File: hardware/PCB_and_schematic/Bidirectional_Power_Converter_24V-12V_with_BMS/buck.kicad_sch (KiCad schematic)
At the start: 0 parts

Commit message: Drawning schematic for buck/boost converter
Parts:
- added U2: LM358, symbol Amplifier_Operational:LM358
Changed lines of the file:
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@@
 	(generator_version "8.0")
 	(paper "A4")
+	(symbol
+		(lib_id "Amplifier_Operational:LM358")
+		(at 219.71 140.97 180)
+		(unit 2)
+		(exclude_from_sim no)
+		(in_bom yes)
+		(on_board yes)
+		(dnp no)
+		(fields_autoplaced yes)
+		(property "Reference" "U2"
+			(at 219.71 130.81 0)
+			(effects
+				(font
+					(size 1.27 1.27)
+				)
+			)
+		)
+		(property "Value" "LM358"
+			(at 219.71 133.35 0)
+			(effects
+				(font
+					(size 1.27 1.27)
+				)
+			)
+		)
+		(property "Footprint" ""
+			(at 219.71 140.97 0)
+			(effects
+				(font
+					(size 1.27 1.27)
+				)
+				(hide yes)
+			)
+		)
+		(property "Datasheet" "http://www.ti.com/lit/ds/symlink/lm2904-n.pdf"
+			(at 219.71 140.97 0)
+			(effects
+				(font
+					(size 1.27 1.27)
+				)
+				(hide yes)
+			)
+		)
+		(property "Description" "Low-Power, Dual Operational Amplifiers, DIP-8/SOIC-8/TO-99-8"
+			(at 219.71 140.97 0)
+			(effects
+				(font
+					(size 1.27 1.27)
+				)
+				(hide yes)
+			)
+		)
+		(pin "1"
+		)
+		(pin "6"
+		)
+		(pin "5"
+		)
+		(pin "8"
+		)
+		(pin "3"
+		)
+		(pin "2"
+		)
+		(pin "7"
+		)
+		(pin "4"
+		)
+		(instances
+			(project "Bidirectional_Power_Converter_24V-12V_with_BMS"
+				(path "/57ff2453-26d1-489b-aa83-9af273df178f/81802b0c-d137-483c-9072-3d8784bb4773/ebfaa78a-1358-458a-b207-86dd3b22cb8b"
+					(reference "U2")
+					(unit 2)
+				)
+			)
+		)
+	)
 )

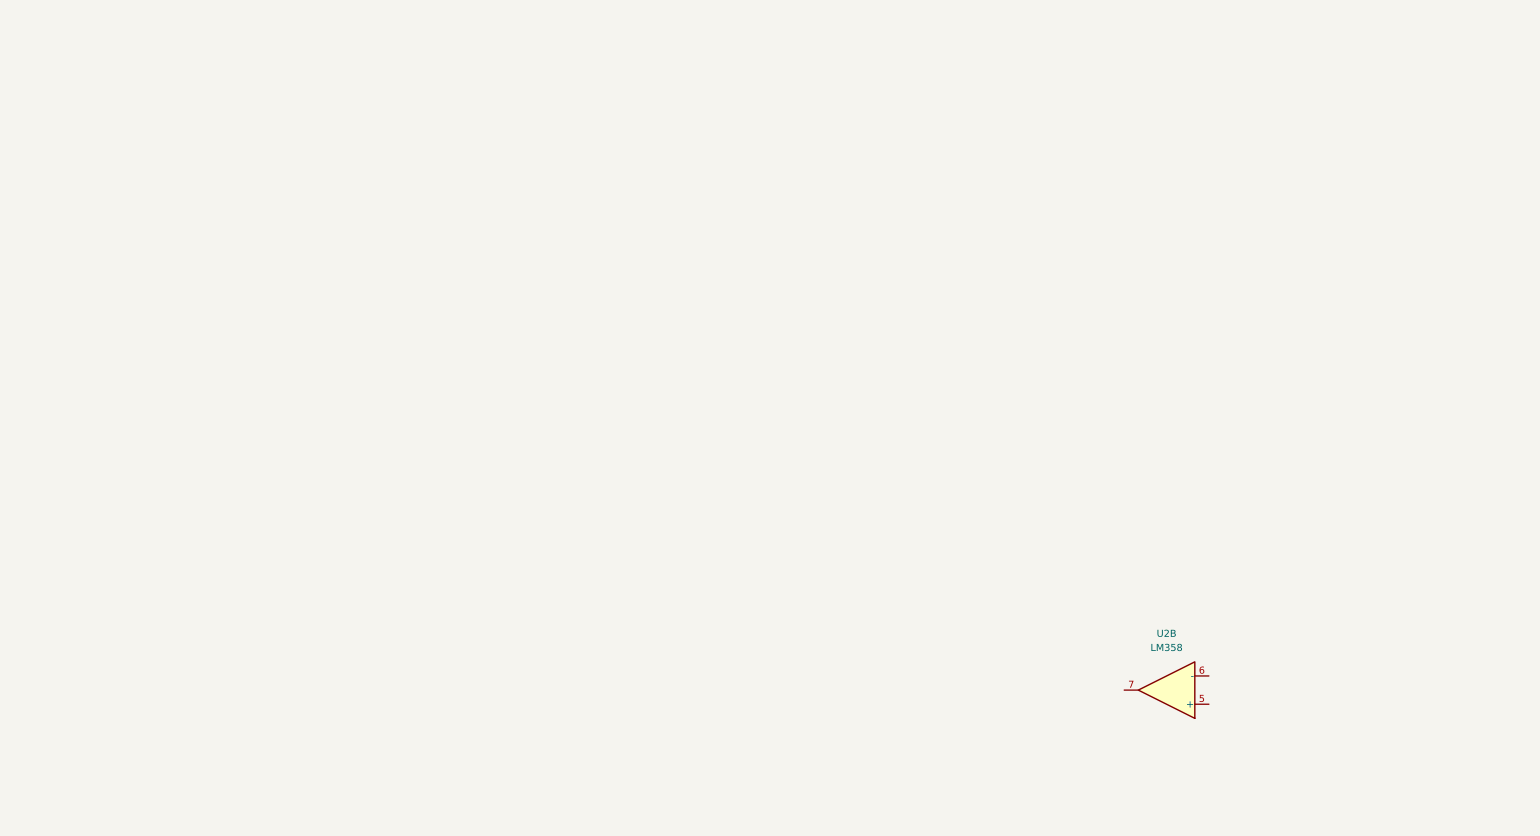
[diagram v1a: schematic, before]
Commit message: Schematic for buck/boost conv
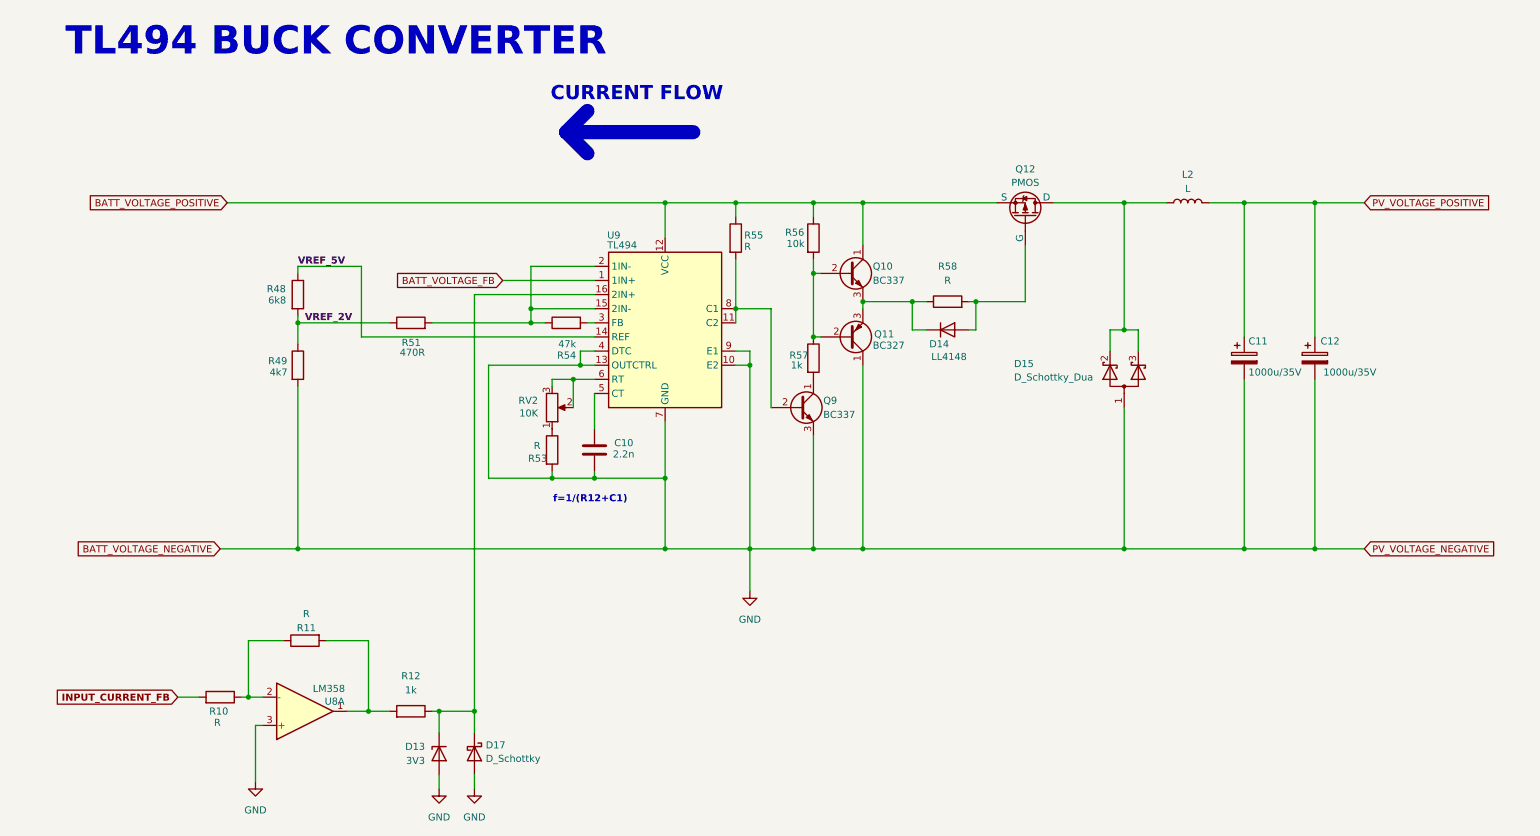
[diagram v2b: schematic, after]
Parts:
- removed U2: LM358, symbol Amplifier_Operational:LM358
- added C10: 2.2n, symbol Device:C
- added C11, C12: 1000u/35V, symbol Device:C_Polarized
- added D13: 3V3, symbol Device:D_Zener
- added D14: LL4148, Diode_SMD:D_MiniMELF, symbol Diode:LL4148
- added D15: D_Schottky_Dua, symbol Device:D_Schottky_Dual_CommonAnode_AKK_Parallel
- added D17: D_Schottky, symbol Device:D_Schottky
- added L2: L, symbol Device:L
- added Q10, Q9: BC337, Package_TO_SOT_THT:TO-92_Inline, symbol Transistor_BJT:BC337
- added Q11: BC327, Package_TO_SOT_THT:TO-92_Inline, symbol Transistor_BJT:BC327
- added Q12: PMOS, symbol Simulation_SPICE:PMOS
- added R10, R11, R53, R55, R58: R, Resistor_SMD:R_0805_2012Metric, symbol Device:R
- added R12, R57: 1k, Resistor_SMD:R_0805_2012Metric, symbol Device:R
- added R48: 6k8, Resistor_SMD:R_0805_2012Metric, symbol Device:R
- added R49: 4k7, Resistor_SMD:R_0805_2012Metric, symbol Device:R
- added R51: 470R, Resistor_SMD:R_0805_2012Metric, symbol Device:R
- added R54: 47k, Resistor_SMD:R_0805_2012Metric, symbol Device:R
- added R56: 10k, Resistor_SMD:R_0805_2012Metric, symbol Device:R
- added RV2: 10K, symbol Device:R_Potentiometer
- added U8: LM358, symbol Amplifier_Operational:LM358
- added U9: TL494, symbol Regulator_Controller:TL494
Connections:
- new net: D15.2 (K), D15.3 (K), L2.1, Q12.1 (D)
- new net: C10.1, U9.5 (CT)
- new net: Q9.1 (C), R57.2
- new net: Q9.2 (B), R55.2, U9.11 (C2), U9.8 (C1)
- new net: Q10.2 (B), Q11.2 (B), R56.2, R57.1
- new net: D14.1 (K), Q10.3 (E), Q11.3 (E), R58.1
- new net: R53.1, RV2.1
- new net: D13.1 (K), D17.1 (K), R12.1, U9.16 (2IN+)
- new net: D14.2 (A), Q12.2 (G), R58.2
- new net: R10.1, R11.1, U8.2 (-)
- new net: R11.2, R12.2, U8.1
- new net: RV2.2, RV2.3, U9.6 (RT)
- new net: R51.2, R54.1, U9.15 (2IN-), U9.2 (1IN-)
- new net: R54.2, U9.3 (FB)
- new net BATT_VOLTAGE_FB: U9.1 (1IN+)
- new net BATT_VOLTAGE_POSITIVE: Q10.1 (C), Q12.3 (S), R55.1, R56.1, U9.12 (VCC)
- new net GND: C10.2, C11.2, C12.2, D13.2 (A), D15.1 (A), D17.2 (A), Q11.1 (C), Q9.3 (E), R49.2, R53.2, U8.3 (+), U9.10 (E2), U9.13 (OUTCTRL), U9.4 (DTC), U9.7 (GND), U9.9 (E1)
- new net INPUT_CURRENT_FB: R10.2
- new net PV_VOLTAGE_POSITIVE: C11.1, C12.1, L2.2
- new net VREF_2V: R48.2, R49.1, R51.1
- new net VREF_5V: R48.1, U9.14 (REF)
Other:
- note added: "CURRENT FLOW"
- note added: "TL494 BUCK CONVERTER"
- note added: "f=1/(R12+C1)"

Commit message: buck boost conv. progrress
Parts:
- added Q13: BC337, Package_TO_SOT_THT:TO-92_Inline, symbol Transistor_BJT:BC337
- added R43: 0R, Resistor_SMD:R_0805_2012Metric, symbol Device:R
- added R50, R52: 10k, Resistor_SMD:R_0805_2012Metric, symbol Device:R
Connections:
- net BATT_VOLTAGE_POSITIVE: now also C11.1, C12.1, L2.2; no longer Q10.1 (C), Q12.3 (S), R55.1, R56.1, U9.12 (VCC)
- net GND: now also Q13.3 (E); no longer U9.4 (DTC)
- net PV_VOLTAGE_POSITIVE: no longer C11.1, C12.1, L2.2
- net VREF_5V: now also R50.1
- net at Q9.2 (B), R55.2, U9.11 (C2)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: now also R43.2
- net at Q10.2 (B), Q11.2 (B), R56.2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: now also R43.1
- net BUCK_CURRENT_FB: now reaches D13.1 (K), D17.1 (K), R12.1, U9.16 (2IN+)
- net INPUT_CURRENT_FB renamed BATT_CURRENT_SHUNT_FB
- new net: Q10.1 (C), Q12.3 (S), R55.1, R56.1, U9.12 (VCC)
- new net: Q13.1 (C), R50.2, U9.4 (DTC)
- new net: Q13.2 (B), R52.2
- new net ENABLE_BUCK: R52.1

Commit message: buck-boost conv update
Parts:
- C4: renamed from C10; footprint (none) -> Capacitor_SMD:C_0805_2012Metric_Pad1.18x1.45mm_HandSolder
- D6: renamed from D13; footprint (none) -> Diode_SMD:D_MiniMELF
- D7: renamed from D17; footprint (none) -> Diode_SMD:D_MiniMELF
- D9: renamed from D15; footprint (none) -> My-Footprints:TO-220-3_Vertical-little-bigger pads
- Q10: renamed from Q12; footprint (none) -> My-Footprints:TO-220-3_Vertical-little-bigger pads
- U3: renamed from U8; footprint (none) -> Package_DIP:CERDIP-8_W7.62mm_SideBrazed_LongPads
- U4: renamed from U9; footprint (none) -> Package_DIP:CERDIP-16_W7.62mm_SideBrazed_LongPads
- renumbered C11 to C5, C12 to C6, D14 to D8, Q13 to Q6, Q9 to Q7, Q10 to Q8, Q11 to Q9, R10 to R28, R48 to R29, R49 to R30, R11 to R31, R52 to R32, R50 to R33, R51 to R34, R12 to R35, R53 to R36, R54 to R37, R55 to R38, R43 to R39, R56 to R40, R57 to R41, R58 to R42

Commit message: buck boost progress
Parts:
- added C6: 100n, Resistor_SMD:R_0805_2012Metric_Pad1.20x1.40mm_HandSolder, symbol Device:C
- C8: renamed from C5; footprint (none) -> Capacitor_THT:CP_Radial_D10.0mm_P3.50mm
- C9: renamed from C6; footprint (none) -> Capacitor_THT:CP_Radial_D10.0mm_P3.50mm
- L2: footprint (none) -> Inductor_THT:L_Toroid_Vertical_L28.6mm_W14.3mm_P11.43mm_Bourns_5700
- RV2: footprint (none) -> Potentiometer_THT:Potentiometer_Runtron_RM-065_Vertical
- renumbered C4 to C7, U3 to U1
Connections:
- net BUCK_CURRENT_FB: now also C6.1
- net GND: now also U1.5 (+), C6.2; no longer U1.3 (+)
- net at R28.1, R31.1: now also U1.6 (-); no longer U1.2 (-)
- net at R31.2, R35.2: now also U1.7; no longer U1.1
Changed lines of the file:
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@@
 	)
 	(junction
+		(at 95.25 157.48)
+		(diameter 0)
+		(color 0 0 0 0)
+	)
+	(junction
 		(at 54.61 142.24)
 		(diameter 0)
@@
 	)
 	(junction
+		(at 100.33 144.78)
+		(diameter 0)
+		(color 0 0 0 0)
+	)
+	(junction
 		(at 97.79 102.87)
 		(diameter 0)
@@
 	(wire
 		(pts
+			(xy 95.25 157.48) (xy 100.33 157.48)
+		)
+		(stroke
+			(width 0)
+			(type default)
+		)
+	)
+	(wire
+		(pts
 			(xy 76.2 144.78) (xy 72.39 144.78)
 		)
@@
 	(wire
 		(pts
-			(xy 88.9 156.21) (xy 88.9 158.75)
-		)
-		(stroke
-			(width 0)
-			(type default)
-		)
-	)
-	(wire
-		(pts
 			(xy 156.21 53.34) (xy 156.21 55.88)
 		)
@@
 	(wire
 		(pts
+			(xy 88.9 156.21) (xy 88.9 157.48)
+		)
+		(stroke
+			(width 0)
+			(type default)
+		)
+	)
+	(wire
+		(pts
 			(xy 105.41 74.93) (xy 107.95 74.93)
 		)
@@
 	(wire
 		(pts
+			(xy 100.33 157.48) (xy 100.33 156.21)
+		)
+		(stroke
+			(width 0)
+			(type default)
+		)
+	)
+	(wire
+		(pts
 			(xy 97.79 82.55) (xy 97.79 102.87)
 		)
@@
 	(wire
 		(pts
+			(xy 100.33 144.78) (xy 102.87 144.78)
+		)
+		(stroke
+			(width 0)
+			(type default)
+		)
+	)
+	(wire
+		(pts
 			(xy 156.21 77.47) (xy 156.21 72.39)
 		)
@@
 	(wire
 		(pts
+			(xy 95.25 157.48) (xy 95.25 158.75)
+		)
+		(stroke
+			(width 0)
+			(type default)
+		)
+	)
+	(wire
+		(pts
 			(xy 80.01 144.78) (xy 76.2 144.78)
 		)
@@
 	(wire
 		(pts
-			(xy 95.25 156.21) (xy 95.25 158.75)
+			(xy 95.25 156.21) (xy 95.25 157.48)
 		)
 		(stroke
@@
 	(wire
 		(pts
-			(xy 95.25 144.78) (xy 102.87 144.78)
+			(xy 95.25 144.78) (xy 100.33 144.78)
 		)
 		(stroke
@@
 	(wire
 		(pts
+			(xy 88.9 157.48) (xy 95.25 157.48)
+		)
+		(stroke
+			(width 0)
+			(type default)
+		)
+	)
+	(wire
+		(pts
+			(xy 100.33 144.78) (xy 100.33 148.59)
+		)
+		(stroke
+			(width 0)
+			(type default)
+		)
+	)
+	(wire
+		(pts
 			(xy 165.1 53.34) (xy 189.23 53.34)
 		)
@@
 	)
 	(symbol
-		(lib_id "power:GND")
-		(at 88.9 158.75 0)
-		(unit 1)
-		(exclude_from_sim no)
-		(in_bom yes)
-		(on_board yes)
-		(dnp no)
-		(fields_autoplaced yes)
-		(property "Reference" "#PWR014"
-			(at 88.9 165.1 0)
-			(effects
-				(font
-					(size 1.27 1.27)
-				)
-				(hide yes)
-			)
-		)
-		(property "Value" "GND"
-			(at 88.9 163.83 0)
-			(effects
-				(font
-					(size 1.27 1.27)
-				)
-			)
-		)
-		(property "Footprint" ""
-			(at 88.9 158.75 0)
-			(effects
-				(font
-					(size 1.27 1.27)
-				)
-				(hide yes)
-			)
-		)
-		(property "Datasheet" ""
-			(at 88.9 158.75 0)
-			(effects
-				(font
-					(size 1.27 1.27)
-				)
-				(hide yes)
-			)
-		)
-		(property "Description" "Power symbol creates a global label with name \"GND\" , ground"
-			(at 88.9 158.75 0)
-			(effects
-				(font
-					(size 1.27 1.27)
-				)
-				(hide yes)
-			)
-		)
-		(pin "1"
-		)
-		(instances
-			(project "Bidirectional_Power_Converter_24V-12V_with_BMS"
-				(path "/57ff2453-26d1-489b-aa83-9af273df178f/81802b0c-d137-483c-9072-3d8784bb4773/ebfaa78a-1358-458a-b207-86dd3b22cb8b"
-					(reference "#PWR014")
-					(unit 1)
-				)
-			)
-		)
-	)
-	(symbol
 		(lib_id "Device:L")
 		(at 223.52 53.34 90)
@@
 			)
 		)
-		(property "Footprint" ""
+		(property "Footprint" "Inductor_THT:L_Toroid_Vertical_L28.6mm_W14.3mm_P11.43mm_Bourns_5700"
 			(at 223.52 53.34 0)
 			(effects
@@
 		(on_board yes)
 		(dnp no)
-		(property "Reference" "C6"
+		(property "Reference" "C9"
 			(at 247.396 78.232 0)
 			(effects
@@
 			)
 		)
-		(property "Footprint" ""
+		(property "Footprint" "Capacitor_THT:CP_Radial_D10.0mm_P3.50mm"
 			(at 247.3452 85.09 0)
 			(effects
@@
 			(project "Bidirectional_Power_Converter_24V-12V_with_BMS"
 				(path "/57ff2453-26d1-489b-aa83-9af273df178f/81802b0c-d137-483c-9072-3d8784bb4773/ebfaa78a-1358-458a-b207-86dd3b22cb8b"
-					(reference "C6")
+					(reference "C9")
 					(unit 1)
 				)
@@
 		(on_board yes)
 		(dnp no)
-		(property "Reference" "C4"
+		(property "Reference" "C7"
 			(at 120.396 96.52 0)
 			(effects
@@
 			(project "Bidirectional_Power_Converter_24V-12V_with_BMS"
 				(path "/57ff2453-26d1-489b-aa83-9af273df178f/81802b0c-d137-483c-9072-3d8784bb4773/ebfaa78a-1358-458a-b207-86dd3b22cb8b"
-					(reference "C4")
+					(reference "C7")
 					(unit 1)
 				)
@@
 		(dnp no)
 		(fields_autoplaced yes)
-		(property "Reference" "#PWR013"
+		(property "Reference" "#PWR014"
 			(at 55.88 163.83 0)
 			(effects
@@
 			(project "Bidirectional_Power_Converter_24V-12V_with_BMS"
 				(path "/57ff2453-26d1-489b-aa83-9af273df178f/81802b0c-d137-483c-9072-3d8784bb4773/ebfaa78a-1358-458a-b207-86dd3b22cb8b"
-					(reference "#PWR013")
+					(reference "#PWR014")
+					(unit 1)
+				)
+			)
+		)
+	)
+	(symbol
+		(lib_id "Device:C")
+		(at 100.33 152.4 0)
+		(mirror y)
+		(unit 1)
+		(exclude_from_sim no)
+		(in_bom yes)
+		(on_board yes)
+		(dnp no)
+		(property "Reference" "C6"
+			(at 108.204 151.13 0)
+			(effects
+				(font
+					(size 1.27 1.27)
+				)
+				(justify left)
+			)
+		)
+		(property "Value" "100n"
+			(at 108.204 153.67 0)
+			(effects
+				(font
+					(size 1.27 1.27)
+				)
+				(justify left)
+			)
+		)
+		(property "Footprint" "Resistor_SMD:R_0805_2012Metric_Pad1.20x1.40mm_HandSolder"
+			(at 99.3648 156.21 0)
+			(effects
+				(font
+					(size 1.27 1.27)
+				)
+				(hide yes)
+			)
+		)
+		(property "Datasheet" "~"
+			(at 100.33 152.4 0)
+			(effects
+				(font
+					(size 1.27 1.27)
+				)
+				(hide yes)
+			)
+		)
+		(property "Description" "Unpolarized capacitor"
+			(at 100.33 152.4 0)
+			(effects
+				(font
+					(size 1.27 1.27)
+				)
+				(hide yes)
+			)
+		)
+		(pin "2"
+		)
+		(pin "1"
+		)
+		(instances
+			(project "Bidirectional_Power_Converter_24V-12V_with_BMS"
+				(path "/57ff2453-26d1-489b-aa83-9af273df178f/81802b0c-d137-483c-9072-3d8784bb4773/ebfaa78a-1358-458a-b207-86dd3b22cb8b"
+					(reference "C6")
 					(unit 1)
 				)
@@
 			)
 		)
-		(property "Footprint" ""
+		(property "Footprint" "Potentiometer_THT:Potentiometer_Runtron_RM-065_Vertical"
 			(at 109.22 90.17 0)
 			(effects
@@
 		(on_board yes)
 		(dnp no)
-		(property "Reference" "C5"
+		(property "Reference" "C8"
 			(at 234.442 78.232 0)
 			(effects
@@
 			)
 		)
-		(property "Footprint" ""
+		(property "Footprint" "Capacitor_THT:CP_Radial_D10.0mm_P3.50mm"
 			(at 234.6452 85.09 0)
 			(effects
@@
 			(project "Bidirectional_Power_Converter_24V-12V_with_BMS"
 				(path "/57ff2453-26d1-489b-aa83-9af273df178f/81802b0c-d137-483c-9072-3d8784bb4773/ebfaa78a-1358-458a-b207-86dd3b22cb8b"
-					(reference "C5")
+					(reference "C8")
 					(unit 1)
 				)
@@
 		(at 64.77 144.78 0)
 		(mirror x)
-		(unit 1)
+		(unit 2)
 		(exclude_from_sim no)
 		(in_bom yes)
 		(on_board yes)
 		(dnp no)
-		(property "Reference" "U3"
+		(property "Reference" "U1"
 			(at 70.104 143.002 0)
 			(effects
@@
 			(project "Bidirectional_Power_Converter_24V-12V_with_BMS"
 				(path "/57ff2453-26d1-489b-aa83-9af273df178f/81802b0c-d137-483c-9072-3d8784bb4773/ebfaa78a-1358-458a-b207-86dd3b22cb8b"
-					(reference "U3")
-					(unit 1)
+					(reference "U1")
+					(unit 2)
 				)
 			)
@@
 		(on_board yes)
 		(dnp no)
-		(fields_autoplaced yes)
 		(property "Reference" "D7"
-			(at 97.282 150.8703 90)
+			(at 95.758 149.352 90)
 			(effects
 				(font
@@
 		)
 		(property "Value" "D_Schottky"
-			(at 97.282 153.2946 90)
+			(at 92.964 149.86 0)
 			(effects
 				(font
-					(size 1.27 1.27)
+					(size 0.6 0.6)
 				)
 				(justify left)
